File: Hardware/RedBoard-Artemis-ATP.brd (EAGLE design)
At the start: 101.6 x 53.3 mm, 149 parts, among them IC3 LM1117, J2 CORTEX_DEBUG, J3 POWER_JACKTOE, J5 USB-C, Q1 1.1A/60V/600mΩ, U3 AP2112-3.3V, U4 ARTEMIS_MODULESMD, U5 CH340C, Y1 32.768kHz

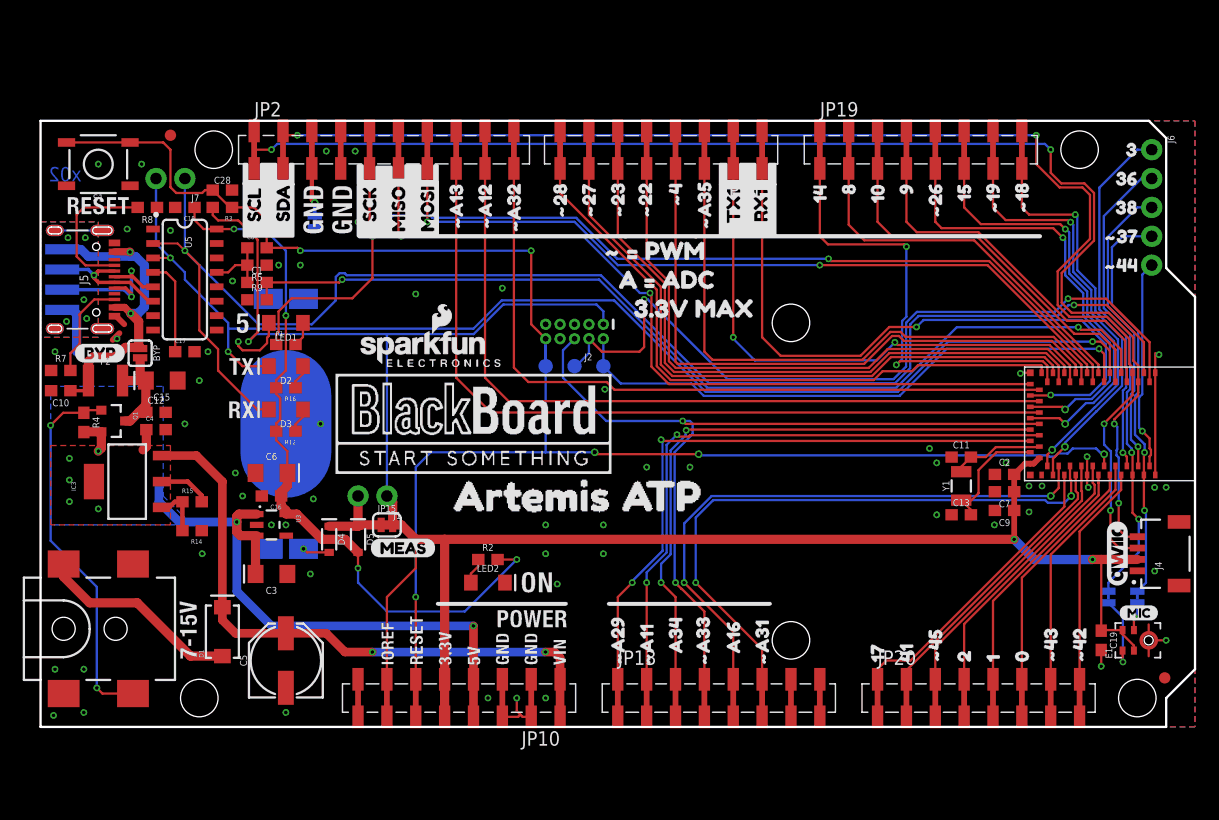
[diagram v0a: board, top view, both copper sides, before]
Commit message: Add SMD Debug. Add PTH holes to each connector.
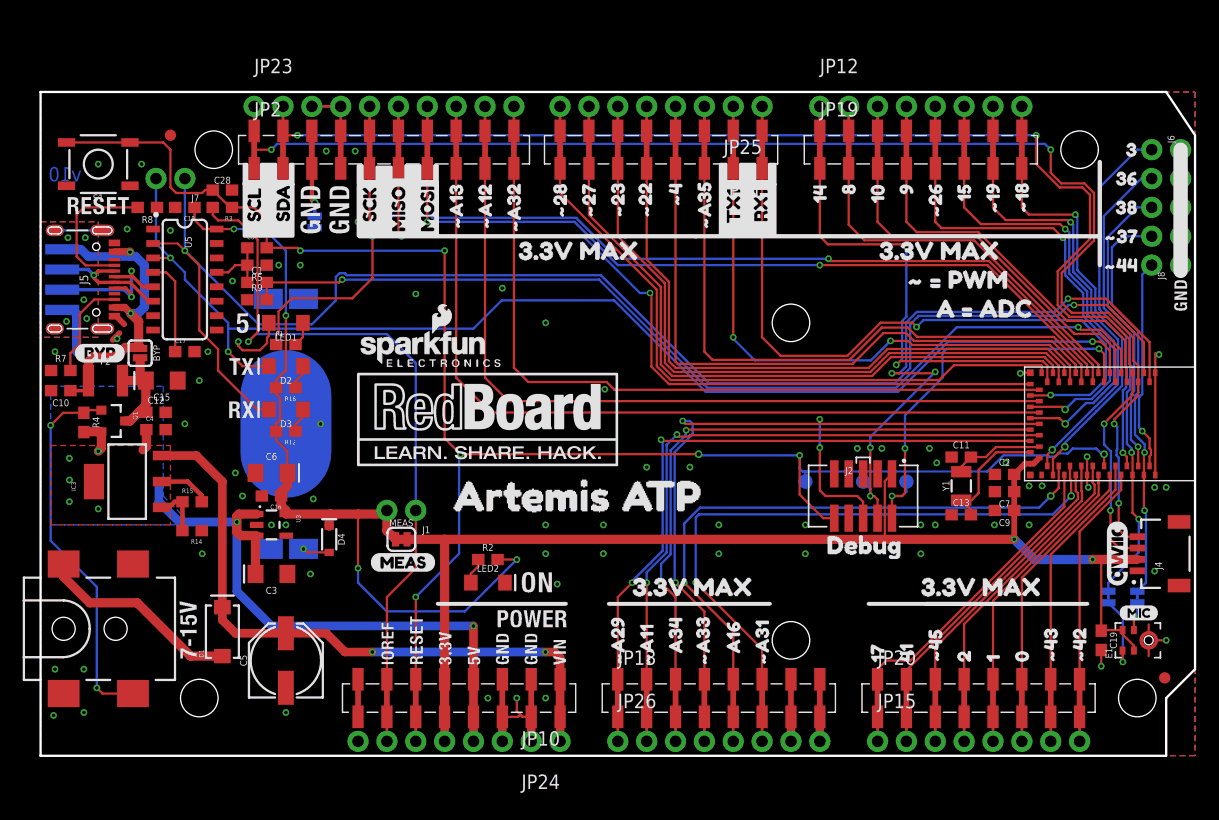
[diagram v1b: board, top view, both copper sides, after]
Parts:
- removed D5: 1A/23V/620mV, SparkFun-DiscreteSemi:SOD-323
- removed U$3: (no value), blackboardlogo:BLACKBOARDLOGO#PNG
- added J8: (no value), SparkFun-Connectors:1X05_NO_SILK
- added JP12, JP25, JP26: JP11, SparkFun-Connectors:1X08_NO_SILK
- added JP23: M10NO_SILK, SparkFun-Connectors:1X10_NO_SILK
- added JP24: (no value), SparkFun-Connectors:1X08_NO_SILK
- added MEAS: (no value), SparkFun-Jumpers:SMT-JUMPER_2_NC_TRACE_SILK
- added U$65, U$73: (no value), buzzard_labels (2):3#3V_MAX2
- added U$76: (no value), buzzard_labels (10):DEBUG2
- D4: value 1A/23V/620mV -> 3A/10V/280mV
- J2: device SparkFun-Connectors:2X5-PTH-1.27MM-NO_SILK -> SparkFun-Connectors:2X5-SMD-1.27MM
- JP15: value (none) -> JP11; device SparkFun-Jumpers:SMT-JUMPER_2_NC_TRACE_SILK -> SparkFun-Connectors:1X08_NO_SILK
- Q1: value 1.1A/60V/600mΩ -> 2.5A/30V/105mΩ
- U$1: device blackboardlogo:BLACKBOARDLOGO#PNG -> buzzard_labels (2):3#3V_MAX2
- moved JP15 47.2 mm to (73.7, -1.27)
- moved J2 29.2 mm to (72.4, 20.3), turned to 0 degrees
- moved TP2 28.5 mm to (76.2, 21.6)
- moved U$69 28.1 mm to (77.5, 36.8)
- moved TP1 27.4 mm to (72.4, 21.6)
- moved U$66 26.8 mm to (74.9, 39.4)
- moved TP3 25.0 mm to (67.3, 21.6)
- moved U$1 19.1 mm to (50.7, 12.3)
- moved U$67 11.4 mm to (40.6, 41.9)
- moved J1 2.84 mm to (33.0, 19.1)
- moved U$70 1.27 mm to (29.0, 14.5)
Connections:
- removed net N$3: D4.C, D5.C, J1.2, JP15.1
- net !RESET: now also JP24.6
- net 3.3V: now also D4.C, J1.2, MEAS.1; no longer D5.A
- net 5V: now also JP24.4
- net AD16: now also JP26.5
- net AD34: now also JP26.3
- net D0: now also JP15.6
- net D1: now also JP15.5
- net D10: now also JP12.3
- net D14: now also JP12.1
- net D15: now also JP12.6
- net D17: now also JP15.1
- net D2: now also JP15.4
- net D40/SDA: now also JP23.2
- net D41: now also JP15.2
- net D8: now also JP12.2
- net D9: now also JP12.4
- net GND: now also J8.1, J8.2, J8.3, J8.4, J8.5, JP13.7A, JP13.7B, JP13.8A, JP13.8B, JP23.3, JP23.4, JP24.2, JP24.3, JP26.7, JP26.8
- net VDD: now also JP24.5, JP24.7, MEAS.2; no longer JP15.2
- net VIN: now also JP24.1
- net ~AD11: now also JP26.2
- net ~AD12: now also JP23.9
- net ~AD13: now also JP23.8
- net ~AD29: now also JP26.1
- net ~AD31: now also JP26.6
- net ~AD32: now also JP23.10
- net ~AD33/SWO: now also JP26.4
- net ~AD35: now also JP25.3
- net ~D18: now also JP12.8
- net ~D19: now also JP12.7
- net ~D22: now also JP25.5
- net ~D23: now also JP25.6
- net ~D24/TXO-1: now also JP25.2
- net ~D25/RXI-1: now also JP25.1
- net ~D26: now also JP12.5
- net ~D27: now also JP25.7
- net ~D28: now also JP25.8
- net ~D39/SCL: now also JP23.1
- net ~D4: now also JP25.4
- net ~D42: now also JP15.8
- net ~D43: now also JP15.7
- net ~D45: now also JP15.3
- net ~D5/SCK: now also JP23.5
- net ~D6/MISO: now also JP23.6
- net ~D7/MOSI: now also JP23.7
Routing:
- net SWDCK: track 70.4 -> 53.8 mm, vias 2 -> 5
- net SWDIO: track 51.9 -> 36.2 mm, vias 1 -> 3
- net GND: track 38.5 -> 51.8 mm, vias 59 -> 68
- net VDD: track 187.1 -> 176.2 mm
- net 3.3V: track 63.9 -> 73.4 mm
- net N$3: track 7.28 -> 0.00 mm
- net ~D39/SCL: track 118.9 -> 121.4 mm
- net ~D25/RXI-1: track 61.6 -> 64.1 mm
- net ~AD35: track 56.6 -> 59.1 mm
- net ~D4: track 58.4 -> 60.8 mm
- net ~D24/TXO-1: track 51.7 -> 53.9 mm
- net ~AD29: track 58.6 -> 60.8 mm
- net VIN: track 54.8 -> 57.0 mm
- net AD34: track 57.0 -> 59.1 mm
- net 5V: track 63.6 -> 65.7 mm
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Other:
- board size 101.6 x 53.3 mm -> 101.6 x 58.4 mm
- board text added: "v10"
- board text removed: "x02"

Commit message: Add silk indicators to PTH pins
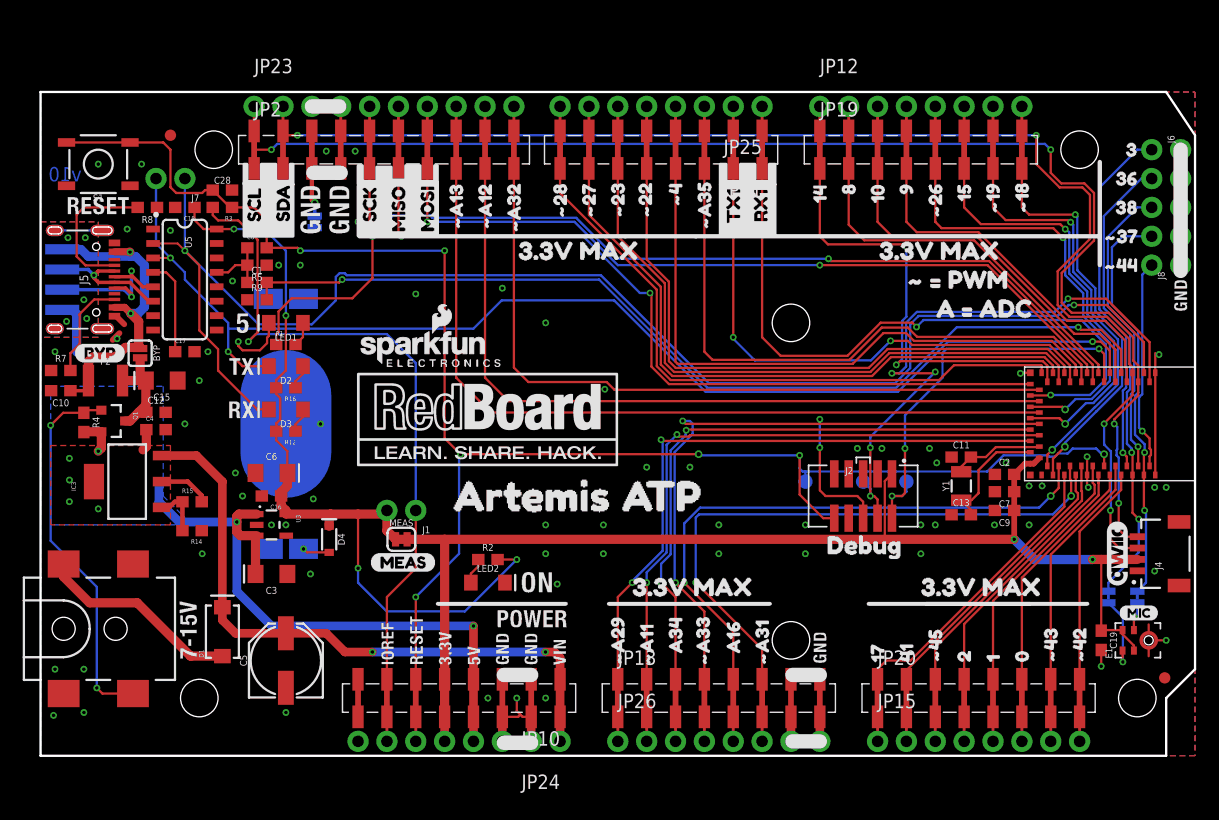
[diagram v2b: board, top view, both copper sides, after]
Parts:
- added LOGO1: SFE_LOGO_NAME_FLAME.1_INCH, SparkFun-Aesthetics:SFE_LOGO_NAME_FLAME_.1
- added U$100: (no value), buzzard_labels (1):#2711
- added U$101: (no value), buzzard_labels (1):#A3213
- added U$102: (no value), buzzard_labels (1):#A1214
- added U$103: (no value), buzzard_labels (1):#A1315
- added U$104: (no value), buzzard_labels (8):MOSI7
- added U$105: (no value), buzzard_labels (8):MISO8
- added U$106: (no value), buzzard_labels (8):SCK9
- added U$107: (no value), buzzard_labels (6):SDA0
- added U$108: (no value), buzzard_labels (6):SCL1
- added U$109: (no value), buzzard_labels (1):#A294
- added U$110: (no value), buzzard_labels (1):#A113
- added U$111: (no value), buzzard_labels (1):A342
- added U$112: (no value), buzzard_labels (6):#A332
- added U$113: (no value), buzzard_labels:A160
- added U$114: (no value), buzzard_labels (1):#A310
- added U$115: (no value), buzzard_labels (2):RX11
- added U$116: (no value), buzzard_labels (2):TX10
- added U$3: (no value), buzzard_labels (9):1720
- added U$74: (no value), buzzard_labels (9):4119
- added U$75: (no value), buzzard_labels (9):#4518
- added U$77: (no value), buzzard_labels (9):217
- added U$78: (no value), buzzard_labels (9):116
- added U$79: (no value), buzzard_labels (9):015
- added U$80: (no value), buzzard_labels (9):#4314
- added U$81: (no value), buzzard_labels (9):#4213
- added U$82: (no value), buzzard_labels (9):140
- added U$83: (no value), buzzard_labels (9):81
- added U$84: (no value), buzzard_labels (9):102
- added U$85: (no value), buzzard_labels (9):93
- added U$86: (no value), buzzard_labels (9):#264
- added U$87: (no value), buzzard_labels (9):155
- added U$88: (no value), buzzard_labels (9):#196
- added U$89: (no value), buzzard_labels (9):#187
- added U$90: (no value), buzzard_labels (9):38
- added U$91: (no value), buzzard_labels (9):369
- added U$92: (no value), buzzard_labels (9):3810
- added U$93: (no value), buzzard_labels (9):#3711
- added U$94: (no value), buzzard_labels (9):#4412
- added U$95: (no value), buzzard_labels (1):#A357
- added U$96: (no value), buzzard_labels (1):#48
- added U$97: (no value), buzzard_labels (1):#229
- added U$98: (no value), buzzard_labels (1):#2310
- added U$99: (no value), buzzard_labels (1):#2812
- moved U$15 35.3 mm to (85.6, 20.3)
- moved U$28 35.3 mm to (70.5, 20.3)
- moved U$4 35.3 mm to (89.9, 19.8)

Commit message: Consolidated to one sch sheet.
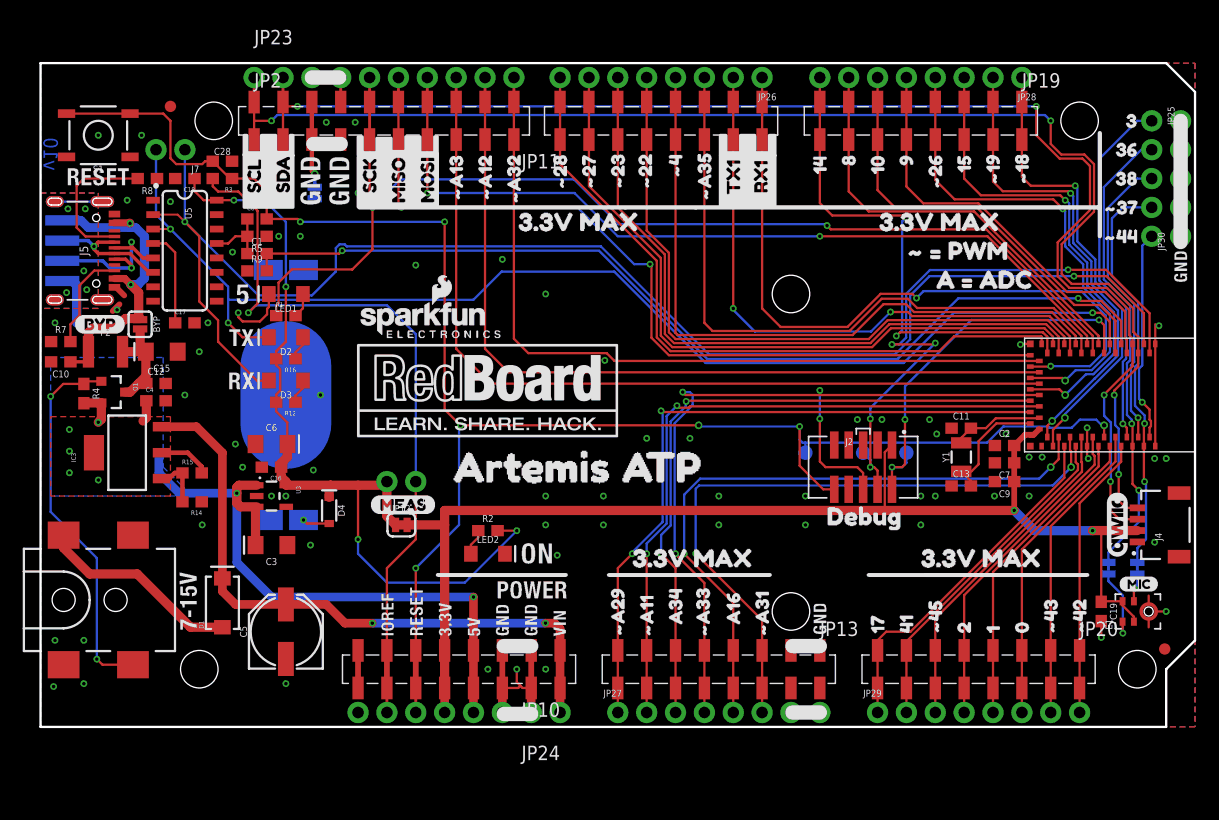
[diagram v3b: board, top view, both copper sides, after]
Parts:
- removed FRAME1: FRAME-LETTER, SparkFun-Aesthetics:CREATIVE_COMMONS
- removed J6, J8: (no value), SparkFun-Connectors:1X05_NO_SILK
- removed JP15: JP11, SparkFun-Connectors:1X08_NO_SILK
- removed MEAS: (no value), SparkFun-Jumpers:SMT-JUMPER_2_NC_TRACE_SILK
- added FRAME3: FRAME-LEDGER, SparkFun-Aesthetics:CREATIVE_COMMONS
- added JP27, JP28, JP29: (no value), SparkFun-Connectors:1X08_NO_SILK
- added JP30: (no value), SparkFun-Connectors:1X05_NO_SILK
- JP10: device SparkFun-Connectors:1X08_SMD_COMBINED -> SparkFun-Connectors:1X08_SMD_COMBINED@1
- JP11, JP13, JP19, JP20: value JP11 -> (none); device SparkFun-Connectors:1X08_SMD_COMBINED -> SparkFun-Connectors:1X08_SMD_COMBINED_NC
- JP12: value JP11 -> MEAS; device SparkFun-Connectors:1X08_NO_SILK -> SparkFun-Jumpers:SMT-JUMPER_2_NC_TRACE_SILK
- JP2: value M10SMD_COMBO -> (none)
- JP23: device SparkFun-Connectors:1X10_NO_SILK -> SparkFun-Connectors:1X10_NO_SILK@1
- JP24: device SparkFun-Connectors:1X08_NO_SILK -> SparkFun-Connectors:1X08_NO_SILK@1
- JP25: value JP11 -> (none); device SparkFun-Connectors:1X08_NO_SILK -> SparkFun-Connectors:1X05_NO_SILK
- JP26: value JP11 -> (none)
- moved JP26 59.8 mm to (63.5, 57.1), turned to 180 degrees
- moved JP12 52.1 mm to (31.8, 17.8)
- moved JP25 34.3 mm to (97.8, 53.3), turned to 270 degrees
- moved JP11 18.0 mm to (45.7, 53.3)
- moved JP13 18.0 mm to (68.6, 5.08)
- moved JP19 18.0 mm to (86.4, 53.3)
- moved JP20 18.0 mm to (91.4, 5.08)
- moved U$70 5.08 mm to (29.0, 19.6)
- moved JP18 2.54 mm to (91.4, 53.3)
- moved JP2 2.54 mm to (18.8, 53.3)
- moved JP6 2.54 mm to (15.2, 53.3)
- moved U$20 2.54 mm to (26.9, 49.3)
- moved U$44 2.54 mm to (94.5, 53.3)
- moved U$67 2.54 mm to (40.6, 44.5)
- moved U$73 2.54 mm to (72.4, 44.5)
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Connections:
- net USBVCC renamed V_USB
- net 3.3V: now also JP12.1; no longer MEAS.1
- net AD16: now also JP13.5, JP13.5@2, JP27.5; no longer JP13.5A, JP13.5B, JP26.5
- net AD34: now also JP13.3, JP13.3@2, JP27.3; no longer JP13.3A, JP13.3B, JP26.3
- net D0: now also JP20.6, JP20.6@2, JP29.6; no longer JP15.6, JP20.6A, JP20.6B
- net D1: now also JP20.5, JP20.5@2, JP29.5; no longer JP15.5, JP20.5A, JP20.5B
- net D10: now also JP19.3, JP19.3@2, JP28.6; no longer JP12.3, JP19.3A, JP19.3B
- net D14: now also JP19.1, JP19.1@2, JP28.8; no longer JP12.1, JP19.1A, JP19.1B
- net D15: now also JP19.6, JP19.6@2, JP28.3; no longer JP12.6, JP19.6A, JP19.6B
- net D17: now also JP20.1, JP20.1@2, JP29.1; no longer JP15.1, JP20.1A, JP20.1B
- net D2: now also JP20.4, JP20.4@2, JP29.4; no longer JP15.4, JP20.4A, JP20.4B
- net D3: now also JP25.1; no longer J6.1
- net D36: now also JP25.2; no longer J6.2
- net D38: now also JP25.3; no longer J6.3
- net D41: now also JP20.2, JP20.2@2, JP29.2; no longer JP15.2, JP20.2A, JP20.2B
- net D8: now also JP19.2, JP19.2@2, JP28.7; no longer JP12.2, JP19.2A, JP19.2B
- net D9: now also JP19.4, JP19.4@2, JP28.5; no longer JP12.4, JP19.4A, JP19.4B
- net GND: now also JP13.7, JP13.7@2, JP13.8, JP13.8@2, JP27.7, JP27.8, JP30.1, JP30.2, JP30.3, JP30.4, JP30.5; no longer J8.1, J8.2, J8.3, J8.4, J8.5, JP13.7A, JP13.7B, JP13.8A, JP13.8B, JP26.7, JP26.8
- net VDD: now also JP12.2; no longer MEAS.2
- net ~AD11: now also JP13.2, JP13.2@2, JP27.2; no longer JP13.2A, JP13.2B, JP26.2
- net ~AD29: now also JP13.1, JP13.1@2, JP27.1; no longer JP13.1A, JP13.1B, JP26.1
- net ~AD31: now also JP13.6, JP13.6@2, JP27.6; no longer JP13.6A, JP13.6B, JP26.6
- net ~AD33/SWO: now also JP13.4, JP13.4@2, JP27.4; no longer JP13.4A, JP13.4B, JP26.4
- net ~AD35: now also JP11.3, JP11.3@2, JP26.3; no longer JP11.3A, JP11.3B, JP25.3
- net ~D18: now also JP19.8, JP19.8@2, JP28.1; no longer JP12.8, JP19.8A, JP19.8B
- net ~D19: now also JP19.7, JP19.7@2, JP28.2; no longer JP12.7, JP19.7A, JP19.7B
- net ~D22: now also JP11.5, JP11.5@2, JP26.5; no longer JP11.5A, JP11.5B, JP25.5
- net ~D23: now also JP11.6, JP11.6@2, JP26.6; no longer JP11.6A, JP11.6B, JP25.6
- net ~D24/TXO-1: now also JP11.2, JP11.2@2, JP26.2; no longer JP11.2A, JP11.2B, JP25.2
- net ~D25/RXI-1: now also JP11.1, JP11.1@2, JP26.1; no longer JP11.1A, JP11.1B, JP25.1
- net ~D26: now also JP19.5, JP19.5@2, JP28.4; no longer JP12.5, JP19.5A, JP19.5B
- net ~D27: now also JP11.7, JP11.7@2, JP26.7; no longer JP11.7A, JP11.7B, JP25.7
- net ~D28: now also JP11.8, JP11.8@2, JP26.8; no longer JP11.8A, JP11.8B, JP25.8
- net ~D37: now also JP25.4; no longer J6.4
- net ~D4: now also JP11.4, JP11.4@2, JP26.4; no longer JP11.4A, JP11.4B, JP25.4
- net ~D42: now also JP20.8, JP20.8@2, JP29.8; no longer JP15.8, JP20.8A, JP20.8B
- net ~D43: now also JP20.7, JP20.7@2, JP29.7; no longer JP15.7, JP20.7A, JP20.7B
- net ~D44: now also JP25.5; no longer J6.5
- net ~D45: now also JP20.3, JP20.3@2, JP29.3; no longer JP15.3, JP20.3A, JP20.3B
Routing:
- net GND: track 51.8 -> 47.5 mm
- net SWDIO: track 36.2 -> 35.0 mm
- net 3.3V: track 73.4 -> 74.7 mm
- net ~D26: track 44.4 -> 43.8 mm
- net ~D5/SCK: track 98.8 -> 99.3 mm
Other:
- outline, holes or cut-outs redrawn
